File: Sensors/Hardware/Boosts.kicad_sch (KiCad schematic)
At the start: 20 parts, among them U11 TPS61092RSAR, U12 LM2623QNHLRQ1

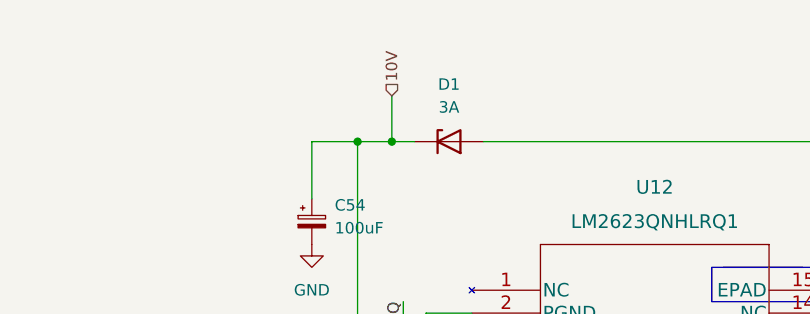
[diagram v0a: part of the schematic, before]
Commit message: 10v rail layout, adc update
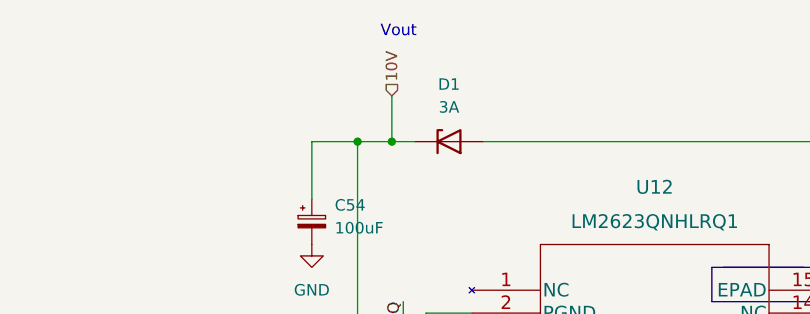
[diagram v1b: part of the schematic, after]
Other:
- note added: "Vout"
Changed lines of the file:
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@@
     (stroke (width 0) (type default) (color 0 0 0 0))
+  )
+  (text "Vout" (at 181.61 43.18 0)
+    (effects (font (size 1.27 1.27)) (justify left bottom))
   )
   (text "Vin" (at 275.59 58.42 0)

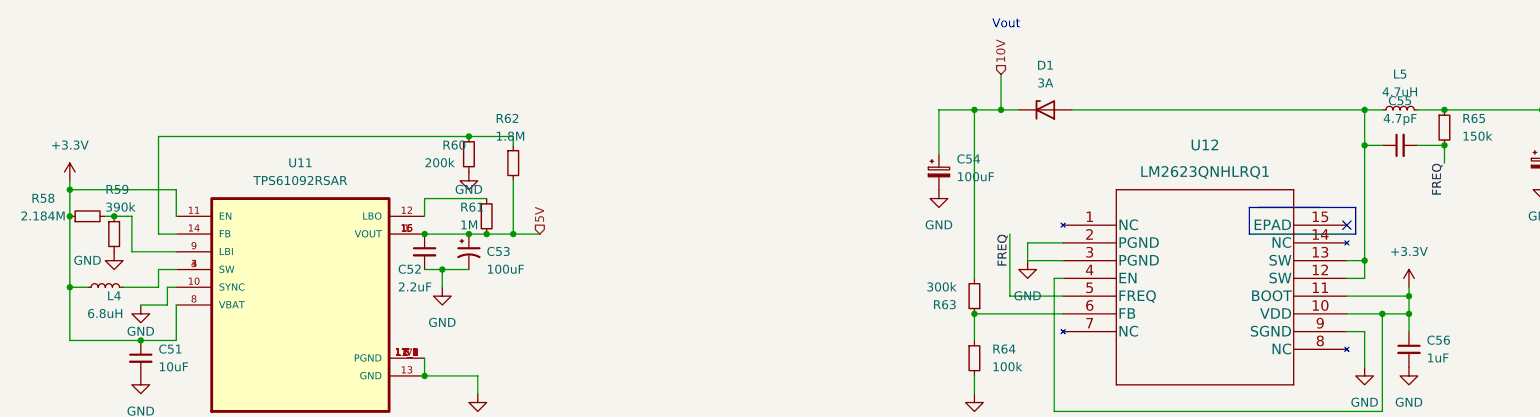
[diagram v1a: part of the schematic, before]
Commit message: ADC connections and KiCAD version update
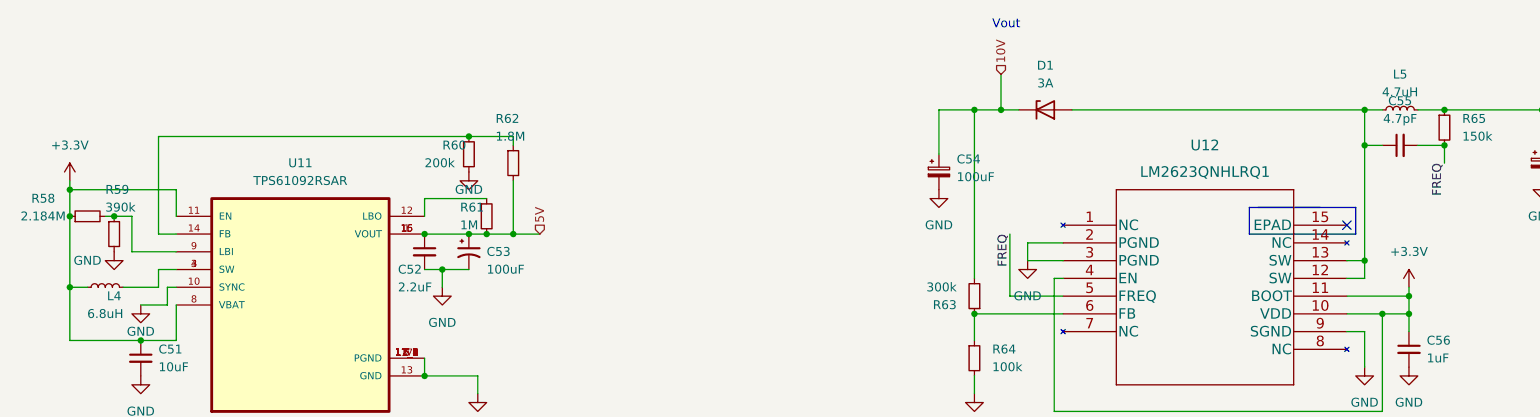
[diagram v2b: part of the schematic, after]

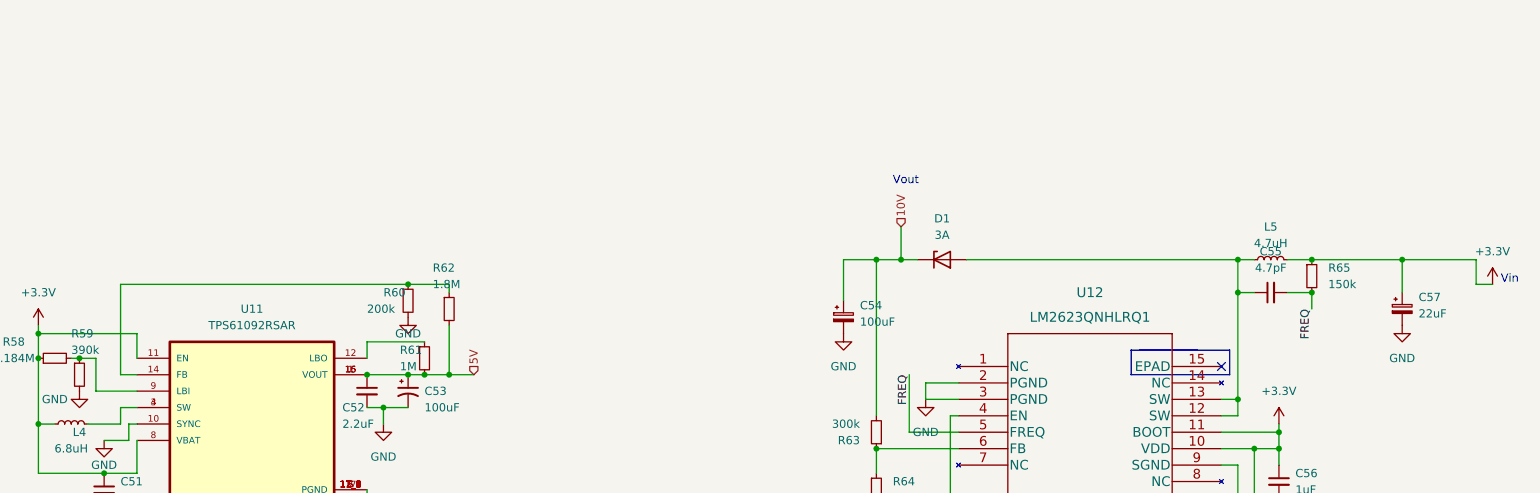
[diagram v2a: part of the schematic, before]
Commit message: Powerlines and LDO layout
updated fp for usb
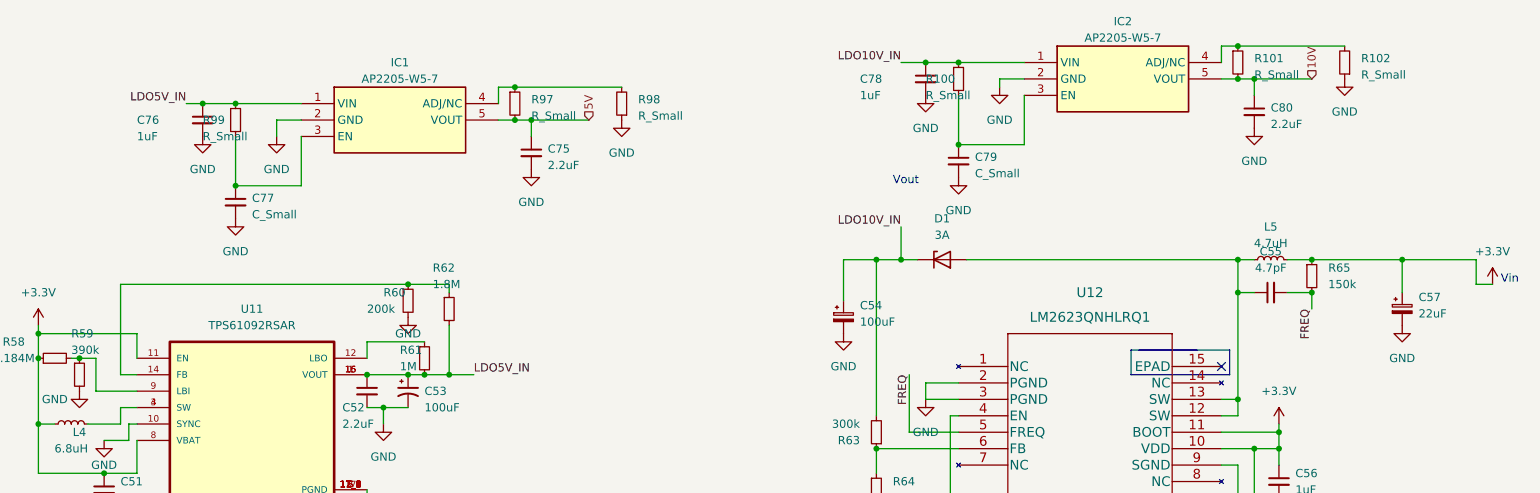
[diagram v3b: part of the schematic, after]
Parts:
- added C75, C80: 2.2uF, Capacitor_SMD:C_0402_1005Metric, symbol Device:C_Small
- added C76, C78: 1uF, Capacitor_SMD:C_0402_1005Metric, symbol Device:C_Small
- added C77, C79: C_Small, Capacitor_SMD:C_0402_1005Metric, symbol Device:C_Small
- added IC1, IC2: AP2205-W5-7, iclr:SOT95P282X145-5N, symbol iclr:AP2205-W5-7
- added R100, R101, R102, R97, R98, R99: R_Small, Resistor_SMD:R_0402_1005Metric, symbol Device:R_Small
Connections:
- net 10V: now also C80.1, IC2.5 (VOUT), R101.2; no longer C54.1, D1.1 (K), R63.2
- net 5V: now also C75.1, IC1.5 (VOUT), R97.2; no longer C52.1, C53.1, R61.2, R62.2, U11.1 (VOUT), U11.15 (VOUT), U11.16 (VOUT)
- net GND: now also C75.2, C76.2, C77.2, C78.2, C79.2, C80.2, IC1.2 (GND), IC2.2 (GND), R102.1, R98.1
- new net: IC1.4 (ADJ/NC), R97.1, R98.2
- new net: C79.1, IC2.3 (EN), R100.2
- new net: IC2.4 (ADJ/NC), R101.1, R102.2
- new net: C77.1, IC1.3 (EN), R99.2
- new net LDO10V_IN: C54.1, C78.1, D1.1 (K), IC2.1 (VIN), R100.1, R63.2
- new net LDO5V_IN: C52.1, C53.1, C76.1, IC1.1 (VIN), R61.2, R62.2, R99.1, U11.1 (VOUT), U11.15 (VOUT), U11.16 (VOUT)

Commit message: added decoupling capacitors to LDOs
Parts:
- added C45 (x2): 10uF, Capacitor_SMD:C_0402_1005Metric, symbol Device:C_Small
- added C49 (x2): 100nF, Capacitor_SMD:C_0402_1005Metric, symbol Device:C_Small
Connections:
- net GND: now also C45.2, C45.2, C49.2, C49.2
- net LDO10V_IN: now also C45.1, C49.1
- net LDO5V_IN: now also C45.1, C49.1
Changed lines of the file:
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@@
   (junction (at 109.22 72.39) (diameter 0) (color 0 0 0 0)
   )
+  (junction (at 139.7 49.53) (diameter 0) (color 0 0 0 0)
+  )
   (junction (at 100.33 72.39) (diameter 0) (color 0 0 0 0)
   )
   (junction (at 237.49 26.67) (diameter 0) (color 0 0 0 0)
   )
+  (junction (at 139.7 54.61) (diameter 0) (color 0 0 0 0)
+  )
   (junction (at 55.88 69.85) (diameter 0) (color 0 0 0 0)
   )
@@
   (junction (at 182.88 54.61) (diameter 0) (color 0 0 0 0)
   )
+  (junction (at 264.16 35.56) (diameter 0) (color 0 0 0 0)
+  )
   (junction (at 74.93 30.48) (diameter 0) (color 0 0 0 0)
   )
   (junction (at 234.95 26.67) (diameter 0) (color 0 0 0 0)
+  )
+  (junction (at 264.16 40.64) (diameter 0) (color 0 0 0 0)
   )
   (junction (at 179.07 54.61) (diameter 0) (color 0 0 0 0)
@@
     (stroke (width 0) (type default))
   )
+  (wire (pts (xy 264.16 34.29) (xy 264.16 35.56))
+    (stroke (width 0) (type default))
+  )
   (polyline (pts (xy 218.44 68.58) (xy 228.6 68.58))
     (stroke (width 0) (type default))
@@
     (stroke (width 0) (type default))
   )
+  (wire (pts (xy 260.35 35.56) (xy 264.16 35.56))
+    (stroke (width 0) (type default))
+  )
   (wire (pts (xy 201.93 26.67) (xy 198.12 26.67))
     (stroke (width 0) (type default))
@@
     (stroke (width 0) (type default))
   )
+  (wire (pts (xy 264.16 35.56) (xy 267.97 35.56))
+    (stroke (width 0) (type default))
+  )
   (wire (pts (xy 57.15 80.01) (xy 62.23 80.01))
     (stroke (width 0) (type default))
   )
+  (wire (pts (xy 260.35 40.64) (xy 264.16 40.64))
+    (stroke (width 0) (type default))
+  )
   (wire (pts (xy 186.69 73.66) (xy 186.69 76.2))
     (stroke (width 0) (type default))
   )
+  (wire (pts (xy 135.89 54.61) (xy 139.7 54.61))
+    (stroke (width 0) (type default))
+  )
   (wire (pts (xy 234.95 21.59) (xy 251.46 21.59))
     (stroke (width 0) (type default))
@@
     (stroke (width 0) (type default))
   )
+  (wire (pts (xy 139.7 54.61) (xy 143.51 54.61))
+    (stroke (width 0) (type default))
+  )
   (wire (pts (xy 120.65 27.94) (xy 123.19 27.94))
     (stroke (width 0) (type default))
   )
+  (wire (pts (xy 264.16 40.64) (xy 267.97 40.64))
+    (stroke (width 0) (type default))
+  )
   (wire (pts (xy 59.69 82.55) (xy 63.5 82.55))
     (stroke (width 0) (type default))
@@
     (stroke (width 0) (type default))
   )
+  (wire (pts (xy 139.7 49.53) (xy 143.51 49.53))
+    (stroke (width 0) (type default))
+  )
   (wire (pts (xy 190.5 97.79) (xy 237.49 97.79))
     (stroke (width 0) (type default))
@@
     (stroke (width 0) (type default))
   )
+  (wire (pts (xy 135.89 49.53) (xy 139.7 49.53))
+    (stroke (width 0) (type default))
+  )
   (wire (pts (xy 242.57 54.61) (xy 246.38 54.61))
     (stroke (width 0) (type default))
@@
   )
   (wire (pts (xy 107.95 92.71) (xy 107.95 95.25))
+    (stroke (width 0) (type default))
+  )
+  (wire (pts (xy 139.7 48.26) (xy 139.7 49.53))
     (stroke (width 0) (type default))
   )
@@
     (effects (font (size 1.27 1.27)) (justify left bottom))
   )
+  (label "LDO10V_IN" (at 264.16 34.29 180) (fields_autoplaced)
+    (effects (font (size 1.27 1.27)) (justify right bottom))
+  )
   (label "LDO10V_IN" (at 182.88 49.53 180) (fields_autoplaced)
     (effects (font (size 1.27 1.27)) (justify right bottom))
@@
   )
   (label "FREQ" (at 184.15 72.39 270) (fields_autoplaced)
+    (effects (font (size 1.27 1.27)) (justify right bottom))
+  )
+  (label "LDO5V_IN" (at 139.7 48.26 180) (fields_autoplaced)
     (effects (font (size 1.27 1.27)) (justify right bottom))
   )
@@
     )
   )
+  (symbol (lib_id "power:GND") (at 264.16 40.64 0) (unit 1)
+    (in_bom yes) (on_board yes) (dnp no) (fields_autoplaced)
+    (property "Reference" "#PWR075" (at 264.16 46.99 0)
+      (effects (font (size 1.27 1.27)) hide)
+    )
+    (property "Value" "GND" (at 264.16 45.72 0)
+      (effects (font (size 1.27 1.27)))
+    )
+    (property "Footprint" "" (at 264.16 40.64 0)
+      (effects (font (size 1.27 1.27)) hide)
+    )
+    (property "Datasheet" "" (at 264.16 40.64 0)
+      (effects (font (size 1.27 1.27)) hide)
+    )
+    (pin "1")
+    (instances
+      (project "sensorboard"
+        (path "/26801cfb-b53b-4a6a-a2f4-5f4986565765/00000000-0000-0000-0000-000061b9f0c0"
+          (reference "#PWR075") (unit 1)
+        )
+        (path "/26801cfb-b53b-4a6a-a2f4-5f4986565765/de0f76c4-1b74-4c96-9fad-1f7da693b4f2"
+          (reference "#PWR0169") (unit 1)
+        )
+      )
+    )
+  )
   (symbol (lib_id "Device:R_Small") (at 234.95 24.13 0) (unit 1)
     (in_bom yes) (on_board yes) (dnp no) (fields_autoplaced)
@@
     )
   )
+  (symbol (lib_id "power:GND") (at 139.7 54.61 0) (unit 1)
+    (in_bom yes) (on_board yes) (dnp no) (fields_autoplaced)
+    (property "Reference" "#PWR075" (at 139.7 60.96 0)
+      (effects (font (size 1.27 1.27)) hide)
+    )
+    (property "Value" "GND" (at 139.7 59.69 0)
+      (effects (font (size 1.27 1.27)))
+    )
+    (property "Footprint" "" (at 139.7 54.61 0)
+      (effects (font (size 1.27 1.27)) hide)
+    )
+    (property "Datasheet" "" (at 139.7 54.61 0)
+      (effects (font (size 1.27 1.27)) hide)
+    )
+    (pin "1")
+    (instances
+      (project "sensorboard"
+        (path "/26801cfb-b53b-4a6a-a2f4-5f4986565765/00000000-0000-0000-0000-000061b9f0c0"
+          (reference "#PWR075") (unit 1)
+        )
+        (path "/26801cfb-b53b-4a6a-a2f4-5f4986565765/de0f76c4-1b74-4c96-9fad-1f7da693b4f2"
+          (reference "#PWR0170") (unit 1)
+        )
+      )
+    )
+  )
   (symbol (lib_id "Device:L_Small") (at 54.61 80.01 90) (unit 1)
     (in_bom yes) (on_board yes) (dnp no)
@@
         (path "/26801cfb-b53b-4a6a-a2f4-5f4986565765/de0f76c4-1b74-4c96-9fad-1f7da693b4f2"
           (reference "C80") (unit 1)
+        )
+      )
+    )
+  )
+  (symbol (lib_id "Device:C_Small") (at 260.35 38.1 0) (unit 1)
+    (in_bom yes) (on_board yes) (dnp no) (fields_autoplaced)
+    (property "Reference" "C45" (at 262.89 36.8362 0)
+      (effects (font (size 1.27 1.27)) (justify left))
+    )
+    (property "Value" "10uF" (at 262.89 39.3762 0)
+      (effects (font (size 1.27 1.27)) (justify left))
+    )
+    (property "Footprint" "Capacitor_SMD:C_0402_1005Metric" (at 260.35 38.1 0)
+      (effects (font (size 1.27 1.27)) hide)
+    )
+    (property "Datasheet" "~" (at 260.35 38.1 0)
+      (effects (font (size 1.27 1.27)) hide)
+    )
+    (pin "1")
+    (pin "2")
+    (instances
+      (project "sensorboard"
+        (path "/26801cfb-b53b-4a6a-a2f4-5f4986565765/00000000-0000-0000-0000-000061b9f0c0"
+          (reference "C45") (unit 1)
+        )
+        (path "/26801cfb-b53b-4a6a-a2f4-5f4986565765/de0f76c4-1b74-4c96-9fad-1f7da693b4f2"
+          (reference "C83") (unit 1)
         )
       )
@@
     )
   )
+  (symbol (lib_id "Device:C_Small") (at 135.89 52.07 0) (unit 1)
+    (in_bom yes) (on_board yes) (dnp no) (fields_autoplaced)
+    (property "Reference" "C45" (at 138.43 50.8062 0)
+      (effects (font (size 1.27 1.27)) (justify left))
+    )
+    (property "Value" "10uF" (at 138.43 53.3462 0)
+      (effects (font (size 1.27 1.27)) (justify left))
+    )
+    (property "Footprint" "Capacitor_SMD:C_0402_1005Metric" (at 135.89 52.07 0)
+      (effects (font (size 1.27 1.27)) hide)
+    )
+    (property "Datasheet" "~" (at 135.89 52.07 0)
+      (effects (font (size 1.27 1.27)) hide)
+    )
+    (pin "1")
+    (pin "2")
+    (instances
+      (project "sensorboard"
+        (path "/26801cfb-b53b-4a6a-a2f4-5f4986565765/00000000-0000-0000-0000-000061b9f0c0"
+          (reference "C45") (unit 1)
+        )
+        (path "/26801cfb-b53b-4a6a-a2f4-5f4986565765/de0f76c4-1b74-4c96-9fad-1f7da693b4f2"
+          (reference "C81") (unit 1)
+        )
+      )
+    )
+  )
   (symbol (lib_id "power:GND") (at 107.95 95.25 0) (unit 1)
     (in_bom yes) (on_board yes) (dnp no) (fields_autoplaced)
@@
     )
   )
+  (symbol (lib_id "Device:C_Small") (at 143.51 52.07 0) (unit 1)
+    (in_bom yes) (on_board yes) (dnp no) (fields_autoplaced)
+    (property "Reference" "C49" (at 146.05 50.8062 0)
+      (effects (font (size 1.27 1.27)) (justify left))
+    )
+    (property "Value" "100nF" (at 146.05 53.3462 0)
+      (effects (font (size 1.27 1.27)) (justify left))
+    )
+    (property "Footprint" "Capacitor_SMD:C_0402_1005Metric" (at 143.51 52.07 0)
+      (effects (font (size 1.27 1.27)) hide)
+    )
+    (property "Datasheet" "~" (at 143.51 52.07 0)
+      (effects (font (size 1.27 1.27)) hide)
+    )
+    (pin "1")
+    (pin "2")
+    (instances
+      (project "sensorboard"
+        (path "/26801cfb-b53b-4a6a-a2f4-5f4986565765/00000000-0000-0000-0000-000061b9f0c0"
+          (reference "C49") (unit 1)
+        )
+        (path "/26801cfb-b53b-4a6a-a2f4-5f4986565765/de0f76c4-1b74-4c96-9fad-1f7da693b4f2"
+          (reference "C82") (unit 1)
+        )
+      )
+    )
+  )
   (symbol (lib_id "power:GND") (at 55.88 74.93 0) (unit 1)
     (in_bom yes) (on_board yes) (dnp no)
@@
         )
       )
+    )
+  )
+  (symbol (lib_id "Device:C_Small") (at 267.97 38.1 0) (unit 1)
+    (in_bom yes) (on_board yes) (dnp no) (fields_autoplaced)
+    (property "Reference" "C49" (at 270.51 36.8362 0)
+      (effects (font (size 1.27 1.27)) (justify left))
+    )
+    (property "Value" "100nF" (at 270.51 39.3762 0)
+      (effects (font (size 1.27 1.27)) (justify left))
+    )
+    (property "Footprint" "Capacitor_SMD:C_0402_1005Metric" (at 267.97 38.1 0)
+      (effects (font (size 1.27 1.27)) hide)
+    )
+    (property "Datasheet" "~" (at 267.97 38.1 0)
+      (effects (font (size 1.27 1.27)) hide)
+    )
+    (pin "1")
+    (pin "2")
+    (instances
+      (project "sensorboard"
+        (path "/26801cfb-b53b-4a6a-a2f4-5f4986565765/00000000-0000-0000-0000-000061b9f0c0"
+          (reference "C49") (unit 1)
+        )
+        (path "/26801cfb-b53b-4a6a-a2f4-5f4986565765/de0f76c4-1b74-4c96-9fad-1f7da693b4f2"
+          (reference "C84") (unit 1)
+        )
+      )
